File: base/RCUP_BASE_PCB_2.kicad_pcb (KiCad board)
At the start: 2 copper layers, 126.2 x 133.1 mm, 79 parts, among them J1 Conn_01x20_Pin, J10 MAIN KILL SWITCH, J11 BatteryIN, J13 MOTOR 2 PWR, J14 MOTOR 4 PWR, J15 24V TO 5V BUCK IN, J16 BASE KILL SWITCH 12V, J17 BASE KILL SWITCH 24V, J18 24V TO 12V BUCK IN, J19 COOLING SYSTEM, J2 Conn_01x20_Pin, J20 COOLING SYSTEM, J21 24V TO 5V BUCK OUT, J22 24V TO 12V BUCK OUT, J23 ARM KILL SWITCH 12V, J24 ARM KILL SWITCH, J25 COOLING SYSTEM, J26 COOLING SYSTEM, J27 EXTRA 12V PORT, J28 EXTRA 5V PORT, J29 EXTRA 24V PORT, J3 Conn_01x20_Pin, J30 Conn_01x03_Pin, J31 Conn_01x03_Pin, J4 Conn_01x20_Pin, J6 MOTOR 1 PWR, J7 MOTOR 3 PWR, J8 STEPPER AND BLDC POWER, J9 JETSON POWER, U3 BNO055, U4 USBLC6-4SC6, U5 USBLC6-4SC6, U6 USBLC6-4SC6, U7 USBLC6-4SC6, U8 USBLC6-4SC6

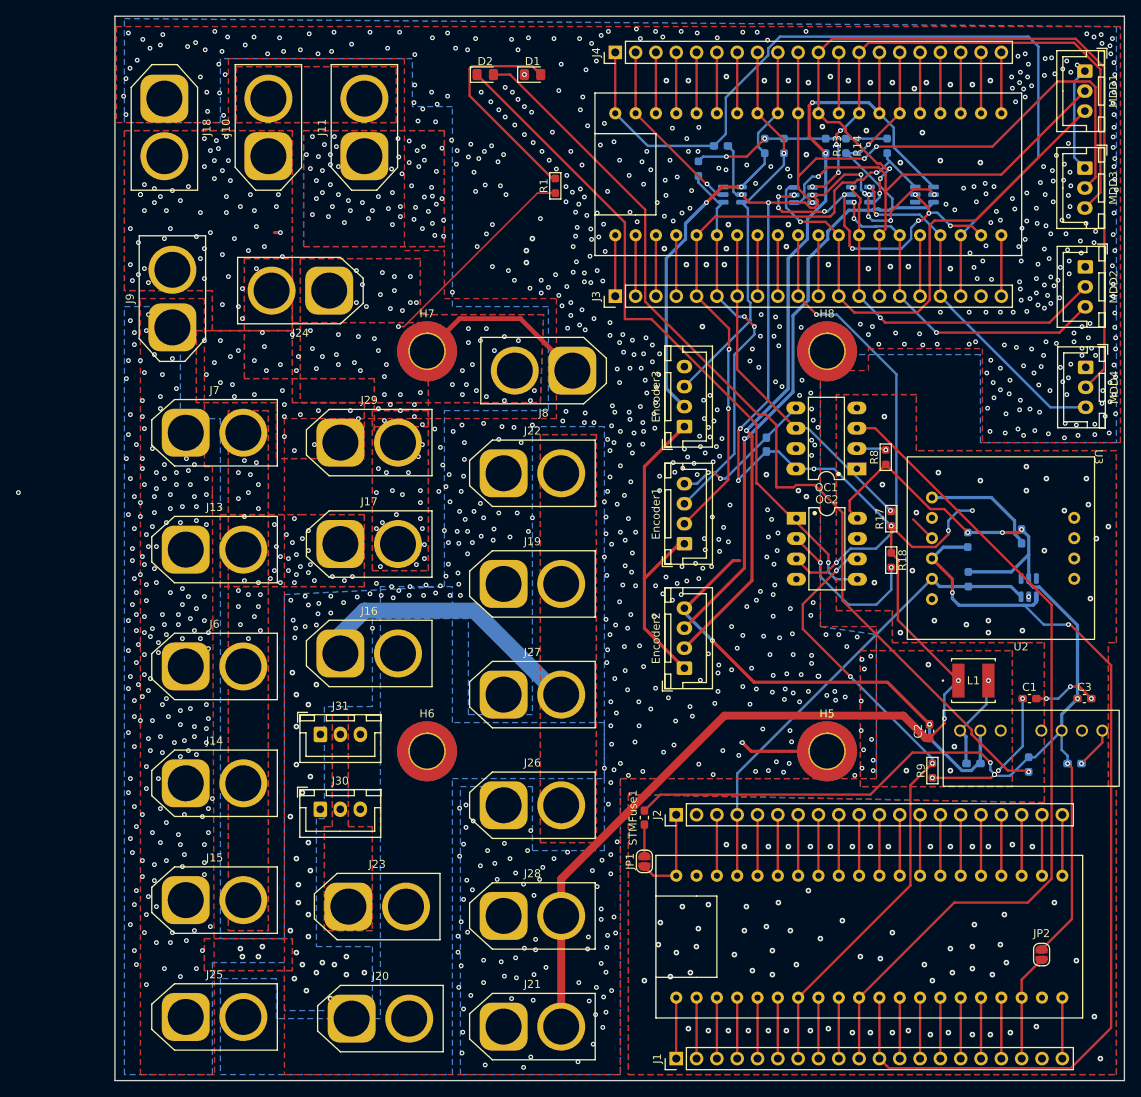
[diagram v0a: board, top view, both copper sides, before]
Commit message: fixed dfm errors some still left
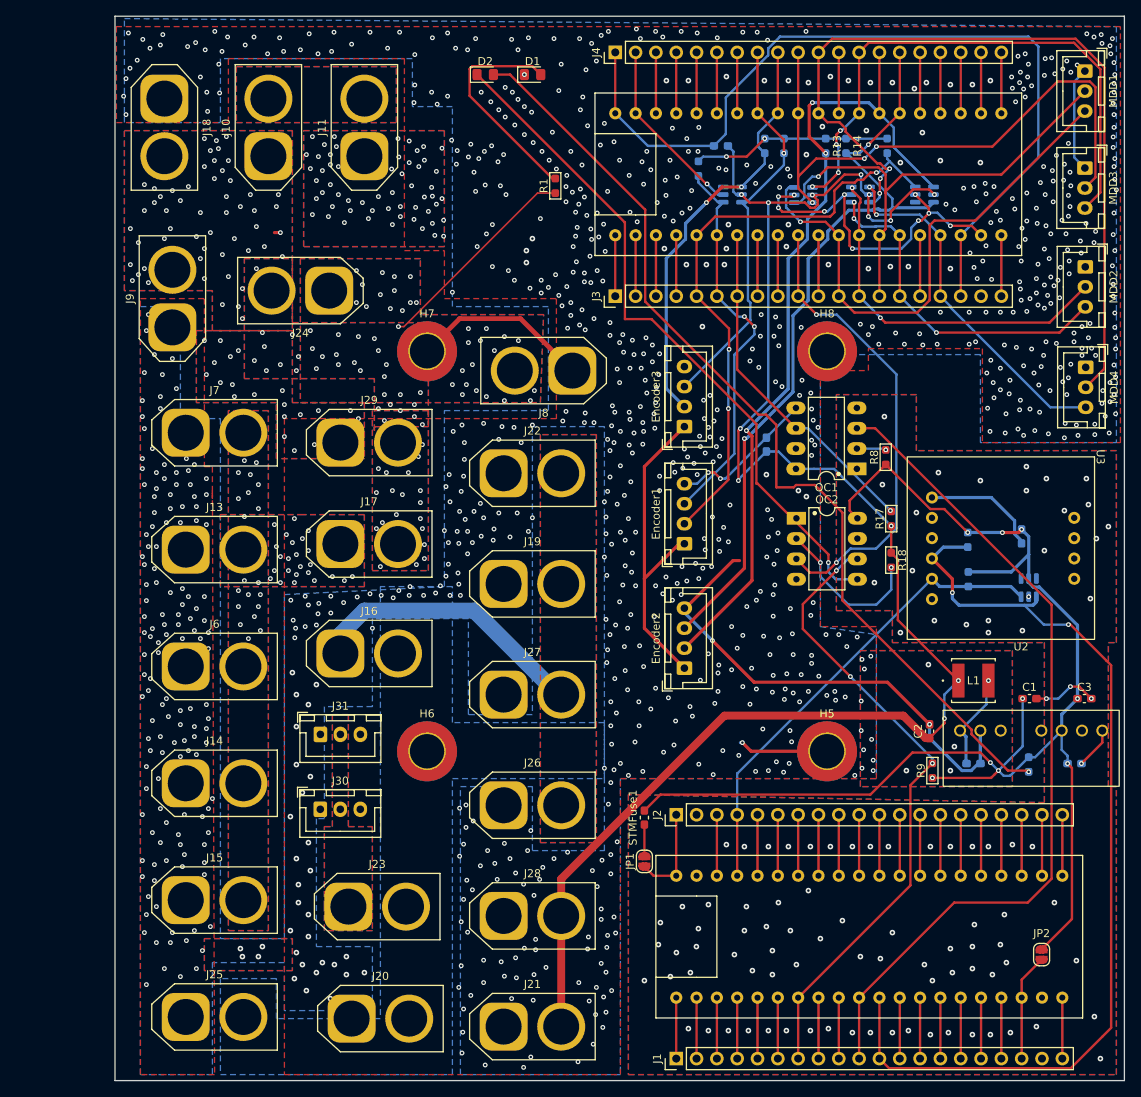
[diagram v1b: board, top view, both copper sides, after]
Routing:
- net 5V: track 223.8 -> 209.7 mm, vias 17 -> 13
- net GND1: track 97.8 -> 94.5 mm
- net 5V_ISO: track 175.1 -> 174.5 mm, vias 12 -> 9
- net STM2_RX: vias 2 -> 1
- net M4PWM: vias 4 -> 2
- net M3PWM: vias 5 -> 4
- net M2PWM: vias 5 -> 3
- net M2DIR: vias 3 -> 2
- net GND: vias 1136 -> 1073
- net ENC3A: vias 3 -> 2
- net ENC2A: vias 4 -> 3
- net ENC1B: vias 4 -> 2
- net BNO_SCL: vias 1 -> 0
- net 5V_NON_ISO_IN: vias 2 -> 0
- net 24V: vias 109 -> 107
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
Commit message: fixed some capacitors
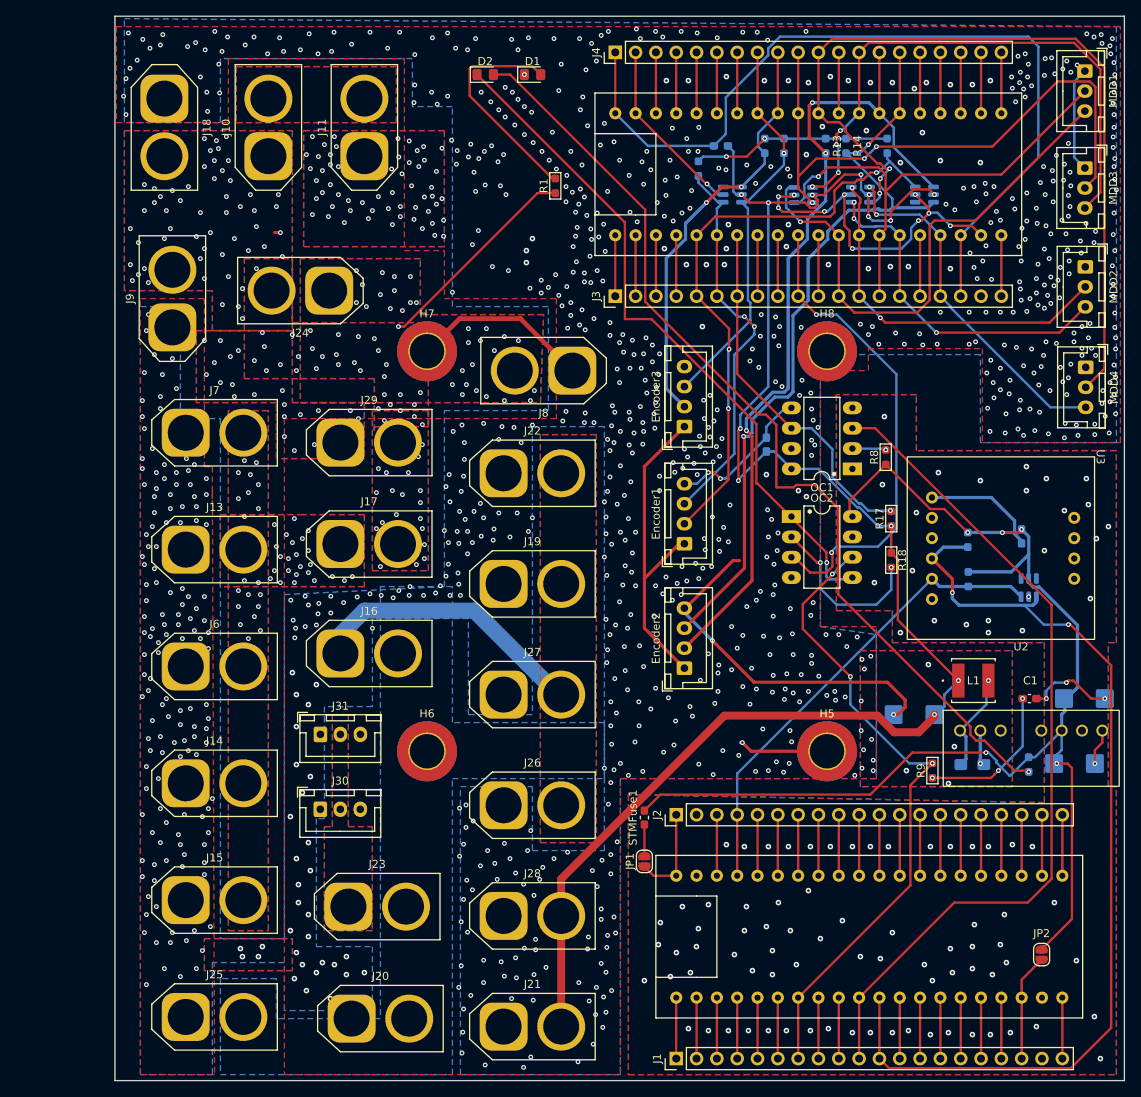
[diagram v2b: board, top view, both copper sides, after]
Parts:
- C2, C3: footprint Capacitor_SMD:C_0603_1608Metric_Pad1.08x0.95mm_HandSolder -> PCM_Capacitor_Tantalum_SMD_AKL:CP_EIA-6032-28_Kemet-C_Pad2.25x2.35mm_HandSolder; moved to B.Cu
- C5: footprint Capacitor_SMD:C_0603_1608Metric_Pad1.08x0.95mm_HandSolder -> Capacitor_Tantalum_SMD:CP_EIA-3216-18_Kemet-A_HandSolder
- C6: footprint Capacitor_SMD:C_0603_1608Metric_Pad1.08x0.95mm_HandSolder -> PCM_Capacitor_Tantalum_SMD_AKL:CP_EIA-6032-28_Kemet-C_Pad2.25x2.35mm_HandSolder
- moved C2 2.84 mm to (215.7, 100.0), turned to 180 degrees
- moved OC2 0.65 mm to (200.4, 75.2)
- moved OC1 0.56 mm to (208.0, 69.3)
- moved C5 0.19 mm to (223.0, 106.2)
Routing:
- net GND: track 195.8 -> 184.8 mm, vias 1073 -> 1074
- net GND1: track 94.5 -> 97.4 mm
- net STM2_RX: track 43.2 -> 45.6 mm
- net STM2_TX: track 58.7 -> 60.7 mm
- net 5V: track 209.7 -> 208.0 mm
- net Net-(OC2-Pad2): track 19.9 -> 21.4 mm
- net ENC2B: track 97.7 -> 99.0 mm
- net STM1_RX: track 79.6 -> 80.8 mm
- net 5V_ISO: track 174.5 -> 175.6 mm, vias 9 -> 8
- net Net-(OC1-Pad2): track 3.68 -> 4.68 mm
- net ENC2A: track 105.7 -> 106.5 mm
- net Net-(U2-Cs): track 5.20 -> 4.50 mm
- net STM1_TX: track 105.6 -> 106.1 mm
- net (no net): vias 12 -> 9
